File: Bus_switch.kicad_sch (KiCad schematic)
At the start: 7 parts, among them J6 Conn_01x04_Pin, U1 SN74CB3Q3384APW

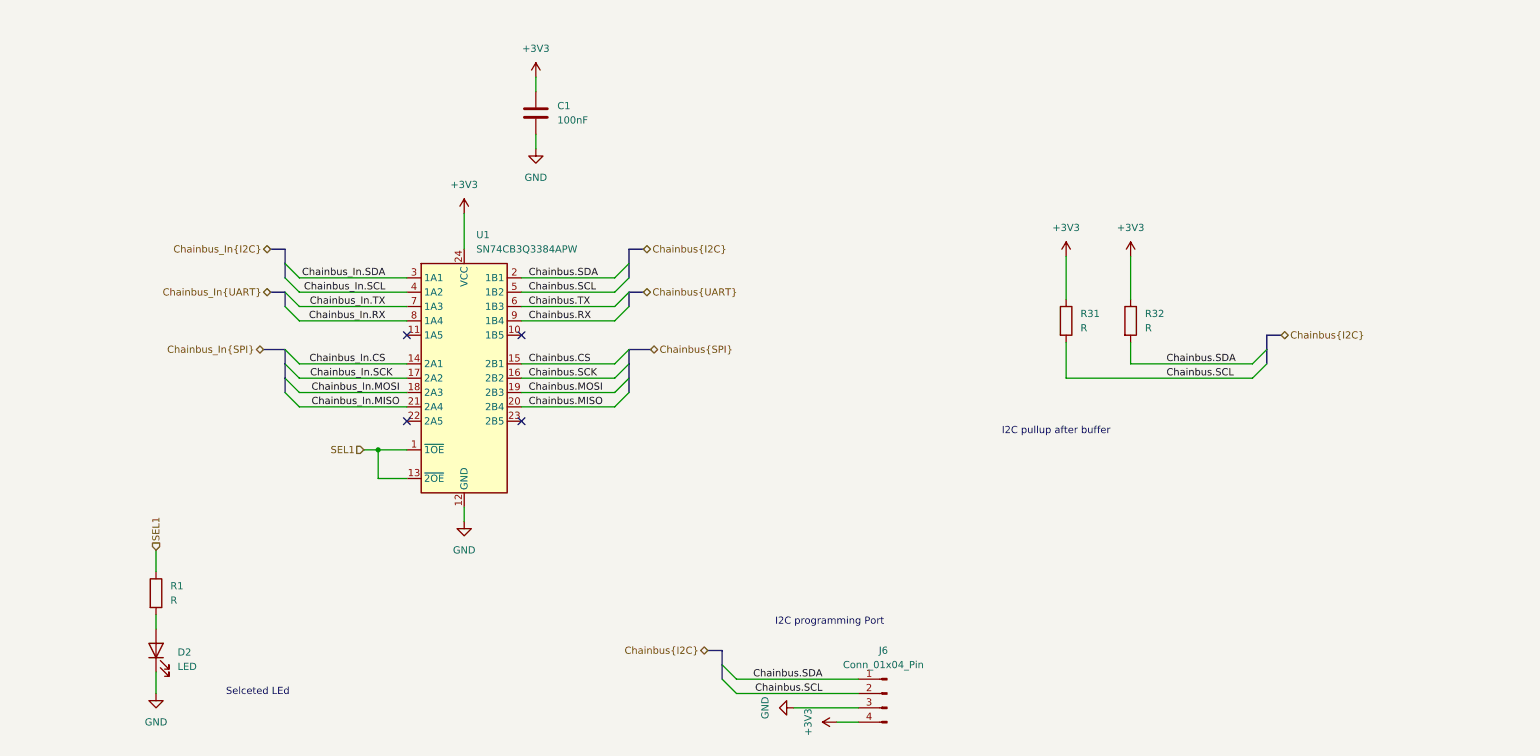
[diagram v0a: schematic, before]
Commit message: finished schematic (without some part numbers)
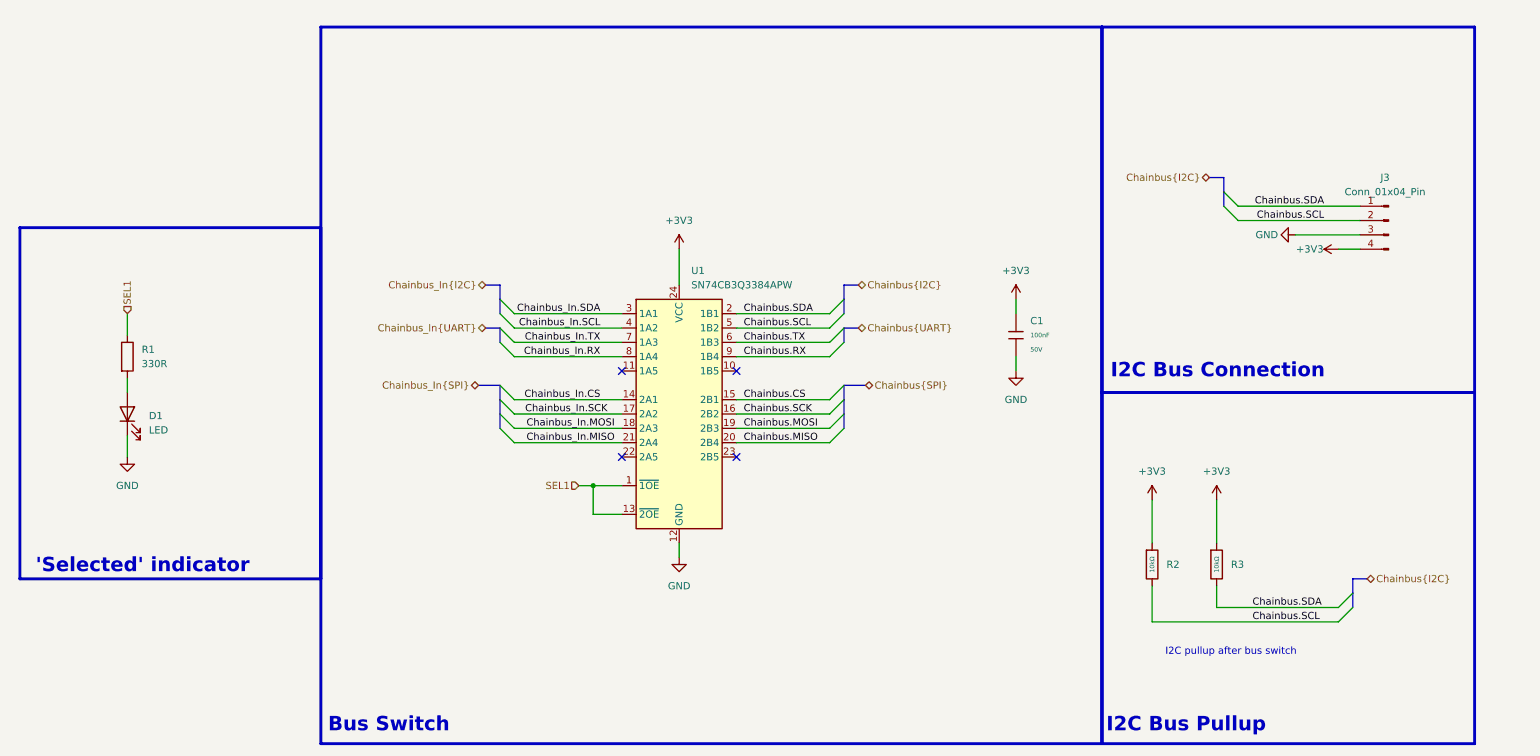
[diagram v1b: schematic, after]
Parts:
- removed C1: 100nF, symbol Device:C
- removed R31, R32: R, symbol Device:R
- added C1: 100nF, PCM_JLCPCB:C_0603, symbol PCM_JLCPCB-Capacitors:0603,100nF
- added R2, R3: 10kΩ, PCM_JLCPCB:R_0402, symbol PCM_JLCPCB-Resistors:0402,10kΩ
- D1: renamed from D2; footprint (none) -> LED_SMD:LED_0603_1608Metric
- J3: renamed from J6; footprint (none) -> Connector_PinHeader_2.54mm:PinHeader_1x04_P2.54mm_Vertical
- R1: value R -> 330R
- U1: LCSC (none) -> C469874
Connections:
- net +3V3: now also C1.1, R2.1, R3.1
- net Chainbus.SCL: now also R2.2
- net Chainbus.SDA: now also R3.2
- net GND: now also C1.2
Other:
- note added: "'Selected' indicator"
- note added: "Bus Switch"
- note added: "I2C Bus Connection"
- note added: "I2C Bus Pullup"
- note added: "I2C pullup after bus switch"
- note removed: "I2C programming Port"
- note removed: "I2C pullup after buffer"
- note removed: "Selceted LEd"
- moved on the sheet: D1, J3, R1, U1

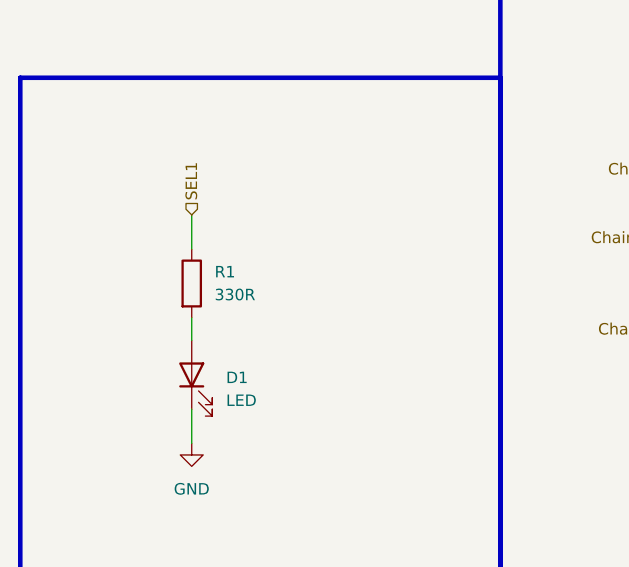
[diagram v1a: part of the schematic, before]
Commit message: initial component placement
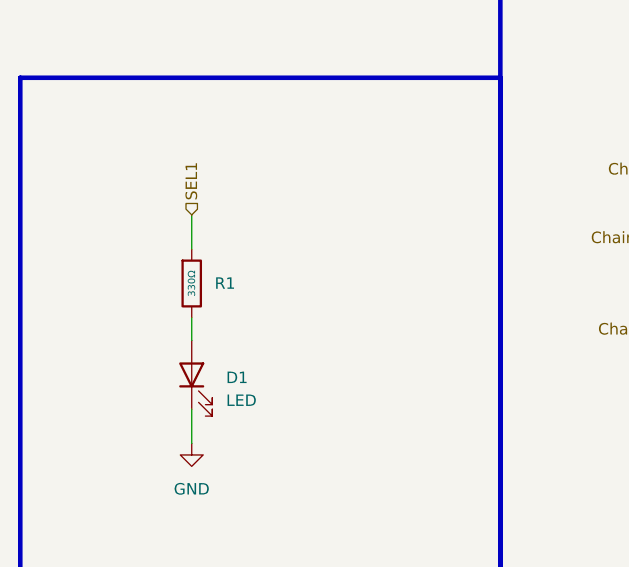
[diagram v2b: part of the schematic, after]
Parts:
- removed R1: 330R, symbol Device:R
- added R1: 330Ω, PCM_JLCPCB:R_0402, symbol PCM_JLCPCB-Resistors:0402,330Ω
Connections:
- net SEL1: now also R1.1
- net at D1.2 (A): now also R1.2
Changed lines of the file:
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@@
+	)
+	(symbol
+		(lib_id "PCM_JLCPCB-Resistors:0402,330Ω")
+		(at 34.29 87.63 0)
+		(unit 1)
+		(exclude_from_sim no)
+		(in_bom yes)
+		(on_board yes)
+		(dnp no)
+		(fields_autoplaced yes)
+		(property "Reference" "R1"
+			(at 36.83 87.6299 0)
+			(effects
+				(font
+					(size 1.27 1.27)
+				)
+				(justify left)
+			)
+		)
+		(property "Value" "330Ω"
+			(at 34.29 87.63 90)
+			(do_not_autoplace yes)
+			(effects
+				(font
+					(size 0.8 0.8)
+				)
+			)
+		)
+		(property "Footprint" "PCM_JLCPCB:R_0402"
+			(at 32.512 87.63 90)
+			(effects
+				(font
+					(size 1.27 1.27)
+				)
+				(hide yes)
+			)
+		)
+		(property "Datasheet" "https://www.lcsc.com/datasheet/lcsc_datasheet_2205311900_UNI-ROYAL-Uniroyal-Elec-0402WGF3300TCE_C25104.pdf"
+			(at 34.29 87.63 0)
+			(effects
+				(font
+					(size 1.27 1.27)
+				)
+				(hide yes)
+			)
+		)
+		(property "Description" "62.5mW Thick Film Resistors 50V ±100ppm/°C ±1% 330Ω 0402 Chip Resistor - Surface Mount ROHS"
+			(at 34.29 87.63 0)
+			(effects
+				(font
+					(size 1.27 1.27)
+				)
+				(hide yes)
+			)
+		)
+		(property "LCSC" "C25104"
+			(at 34.29 87.63 0)
+			(effects
+				(font
+					(size 1.27 1.27)
+				)
+				(hide yes)
+			)
+		)
+		(property "Stock" "1159127"
+			(at 34.29 87.63 0)
+			(effects
+				(font
+					(size 1.27 1.27)
+				)
+				(hide yes)
+			)
+		)
+		(property "Price" "0.004USD"
+			(at 34.29 87.63 0)
+			(effects
+				(font
+					(size 1.27 1.27)
+				)
+				(hide yes)
+			)
+		)
+		(property "Process" "SMT"
+			(at 34.29 87.63 0)
+			(effects
+				(font
+					(size 1.27 1.27)
+				)
+				(hide yes)
+			)
+		)
+		(property "Minimum Qty" "20"
+			(at 34.29 87.63 0)
+			(effects
+				(font
+					(size 1.27 1.27)
+				)
+				(hide yes)
+			)
+		)
+		(property "Attrition Qty" "10"
+			(at 34.29 87.63 0)
+			(effects
+				(font
+					(size 1.27 1.27)
+				)
+				(hide yes)
+			)
+		)
+		(property "Class" "Basic Component"
+			(at 34.29 87.63 0)
+			(effects
+				(font
+					(size 1.27 1.27)
+				)
+				(hide yes)
+			)
+		)
+		(property "Category" "Resistors,Chip Resistor - Surface Mount"
+			(at 34.29 87.63 0)
+			(effects
+				(font
+					(size 1.27 1.27)
+				)
+				(hide yes)
+			)
+		)
+		(property "Manufacturer" "UNI-ROYAL(Uniroyal Elec)"
+			(at 34.29 87.63 0)
+			(effects
+				(font
+					(size 1.27 1.27)
+				)
+				(hide yes)
+			)
+		)
+		(property "Part" "0402WGF3300TCE"
+			(at 34.29 87.63 0)
+			(effects
+				(font
+					(size 1.27 1.27)
+				)
+				(hide yes)
+			)
+		)
+		(property "Resistance" "330Ω"
+			(at 34.29 87.63 0)
+			(effects
+				(font
+					(size 1.27 1.27)
+				)
+				(hide yes)
+			)
+		)
+		(property "Power(Watts)" "62.5mW"
+			(at 34.29 87.63 0)
+			(effects
+				(font
+					(size 1.27 1.27)
+				)
+				(hide yes)
+			)
+		)
+		(property "Type" "Thick Film Resistors"
+			(at 34.29 87.63 0)
+			(effects
+				(font
+					(size 1.27 1.27)
+				)
+				(hide yes)
+			)
+		)
+		(property "Overload Voltage (Max)" "50V"
+			(at 34.29 87.63 0)
+			(effects
+				(font
+					(size 1.27 1.27)
+				)
+				(hide yes)
+			)
+		)
+		(property "Operating Temperature Range" "-55°C~+155°C"
+			(at 34.29 87.63 0)
+			(effects
+				(font
+					(size 1.27 1.27)
+				)
+				(hide yes)
+			)
+		)
+		(property "Tolerance" "±1%"
+			(at 34.29 87.63 0)
+			(effects
+				(font
+					(size 1.27 1.27)
+				)
+				(hide yes)
+			)
+		)
+		(property "Temperature Coefficient" "±100ppm/°C"
+			(at 34.29 87.63 0)
+			(effects
+				(font
+					(size 1.27 1.27)
+				)
+				(hide yes)
+			)
+		)
+		(pin "1"
+		)
+		(pin "2"
+		)
+		(instances
+			(project ""
+				(path "/6596548a-44e0-46d8-8624-fd71cf4a3e17/ec6d73af-72b0-4068-85fb-cca3c5143749"
+					(reference "R1")
+					(unit 1)
+				)
+			)
+		)
 	)
 	(symbol
@@
 					(unit 1)
 				)
-			)
-		)
-	)
-	(symbol
-		(lib_id "Device:R")
-		(at 34.29 87.63 0)
-		(unit 1)
-		(exclude_from_sim no)
-		(in_bom yes)
-		(on_board yes)
-		(dnp no)
-		(fields_autoplaced yes)
-		(property "Reference" "R1"
-			(at 36.83 86.3599 0)
-			(effects
-				(font
-					(size 1.27 1.27)
-				)
-				(justify left)
-			)
-		)
-		(property "Value" "330R"
-			(at 36.83 88.8999 0)
-			(effects
-				(font
-					(size 1.27 1.27)
-				)
-				(justify left)
-			)
-		)
-		(property "Footprint" ""
-			(at 32.512 87.63 90)
-			(effects
-				(font
-					(size 1.27 1.27)
-				)
-				(hide yes)
-			)
-		)
-		(property "Datasheet" "~"
-			(at 34.29 87.63 0)
-			(effects
-				(font
-					(size 1.27 1.27)
-				)
-				(hide yes)
-			)
-		)
-		(property "Description" "Resistor"
-			(at 34.29 87.63 0)
-			(effects
-				(font
-					(size 1.27 1.27)
-				)
-				(hide yes)
-			)
-		)
-		(pin "1"
-		)
-		(pin "2"
-		)
-		(instances
-			(project ""
-				(path "/6596548a-44e0-46d8-8624-fd71cf4a3e17/ec6d73af-72b0-4068-85fb-cca3c5143749"
-					(reference "R1")
-					(unit 1)
-				)

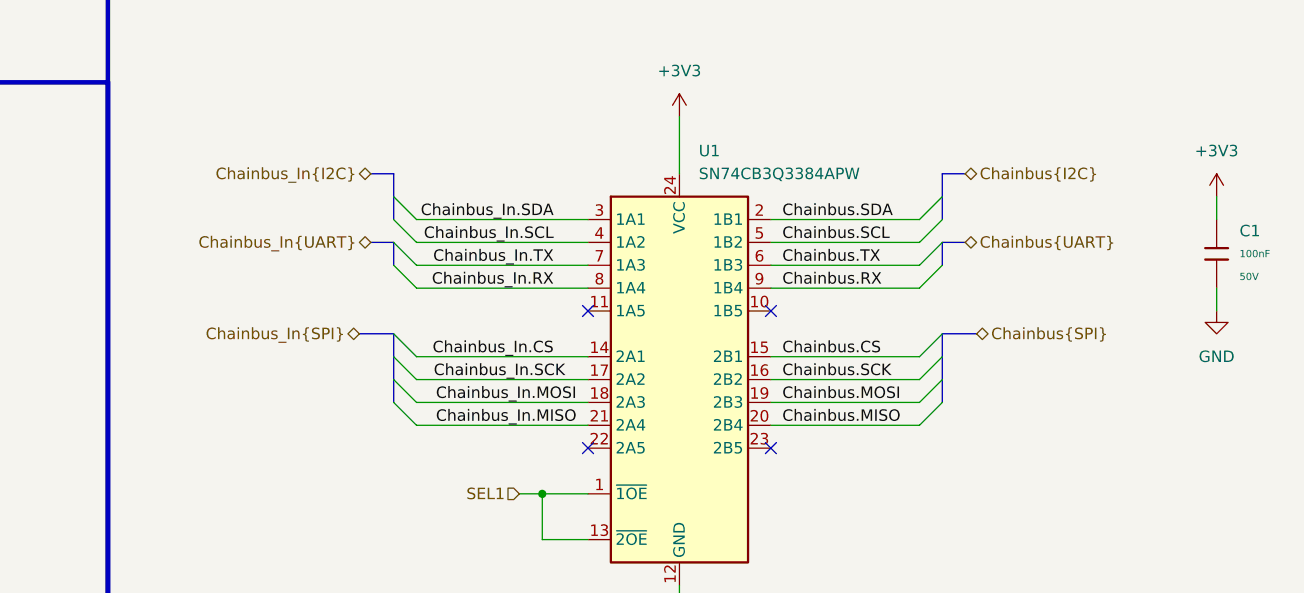
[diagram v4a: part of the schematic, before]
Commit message: Added Routing
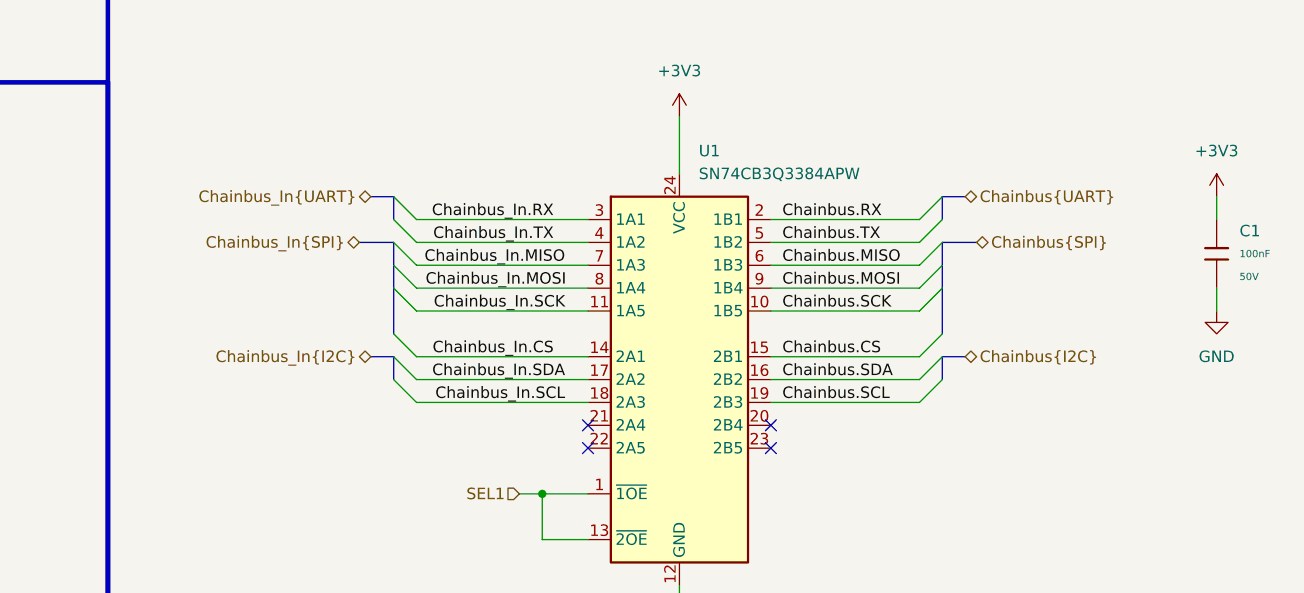
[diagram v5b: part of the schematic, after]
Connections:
- net Chainbus.MISO: now also U1.6 (1B3); no longer U1.20 (2B4)
- net Chainbus.MOSI: now also U1.9 (1B4); no longer U1.19 (2B3)
- net Chainbus.RX: now also U1.2 (1B1); no longer U1.9 (1B4)
- net Chainbus.SCK: now also U1.10 (1B5); no longer U1.16 (2B2)
- net Chainbus.SCL: now also U1.19 (2B3); no longer U1.5 (1B2)
- net Chainbus.SDA: now also U1.16 (2B2); no longer U1.2 (1B1)
- net Chainbus.TX: now also U1.5 (1B2); no longer U1.6 (1B3)
- net Chainbus_In.MISO: now also U1.7 (1A3); no longer U1.21 (2A4)
- net Chainbus_In.MOSI: now also U1.8 (1A4); no longer U1.18 (2A3)
- net Chainbus_In.RX: now also U1.3 (1A1); no longer U1.8 (1A4)
- net Chainbus_In.SCK: now also U1.11 (1A5); no longer U1.17 (2A2)
- net Chainbus_In.SCL: now also U1.18 (2A3); no longer U1.4 (1A2)
- net Chainbus_In.SDA: now also U1.17 (2A2); no longer U1.3 (1A1)
- net Chainbus_In.TX: now also U1.4 (1A2); no longer U1.7 (1A3)

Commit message: updated routing
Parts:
- D1: now not fitted
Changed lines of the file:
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@@
 		(in_bom yes)
 		(on_board yes)
-		(dnp no)
+		(dnp yes)
 		(fields_autoplaced yes)
 		(property "Reference" "D1"

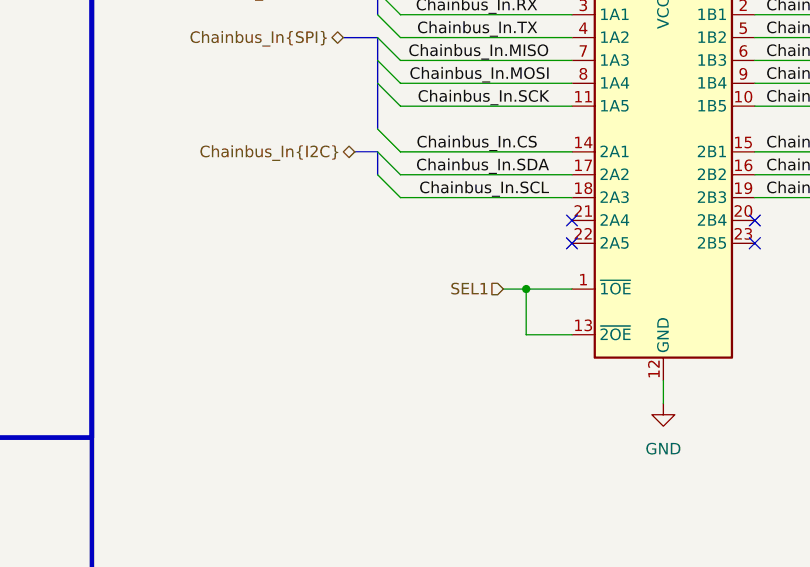
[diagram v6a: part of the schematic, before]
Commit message: added pullup on select
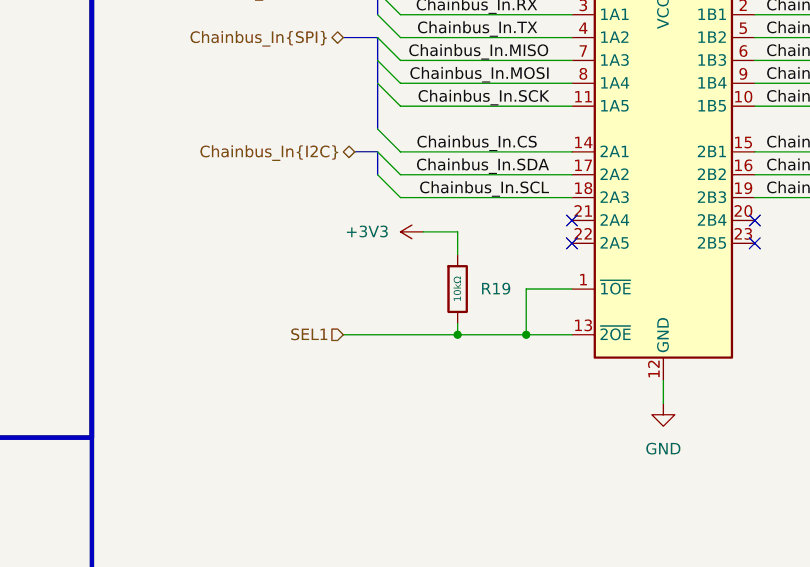
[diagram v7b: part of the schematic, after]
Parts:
- added R19: 10kΩ, PCM_JLCPCB:R_0402, symbol PCM_JLCPCB-Resistors:0402,10kΩ
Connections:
- net +3V3: now also R19.1
- net SEL1: now also R19.2
